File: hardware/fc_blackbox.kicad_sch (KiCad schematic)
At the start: 3 parts

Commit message: Library: every symbol, footprint and 3D model project-local (#28)
* Owner: board cleanup, Core placed on the board

Co-Authored-By: Claude Opus 5.5 <noreply@anthropic.com>

* Library: every symbol, footprint and 3D model project-local

- 3D models: 275 board model paths and 28 lib.pretty footprints pointed at
  KiCad's stock install or at ${OPENDRONE_LIB} (which this machine's KiCad sets
  to a path that does not exist, so 9 models were missing). All now resolve to
  ${KIPRJMOD}/lib.3dshapes; the three missing ones come from the repo's
  KiCad-Library submodule. .wrl replaced by the .step sibling where one exists.
- Symbols: the 14 stock symbols (Device, power, Connector, Connector_Generic,
  MCU_Espressif) copied into lib.kicad_sym from the schematic's own cache and
  relinked as lib:. Four lib symbols refreshed from the schematic (they still
  held the 8fa8d7b copies).
- Pruned: 11 unused footprints, 7 unused symbols, unreferenced model files.
- tools/localise_models.py and tools/localise_symbols.py keep it that way.
- Checks: board diff is model lines only; netlist identical; ERC 31 errors as
  before, lib_symbol_mismatch 9 -> 0.

Co-Authored-By: Claude Opus 5.5 <noreply@anthropic.com>

---------

Co-authored-by: Stan <stan@openaio.local>
Co-authored-by: Claude Opus 5.5 <noreply@anthropic.com>
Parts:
- C36: symbol Device:C -> lib:C
- R34: symbol Device:R -> lib:R
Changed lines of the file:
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@@
 	)
 	(symbol
-		(lib_id "Device:R")
+		(lib_id "lib:R")
 		(at 92.71 60.96 0)
 		(unit 1)
@@
 	)
 	(symbol
-		(lib_id "power:GND")
+		(lib_id "lib:GND")
 		(at 58.42 50.8 270)
 		(unit 1)
@@
 	)
 	(symbol
-		(lib_id "power:GND")
+		(lib_id "lib:GND")
 		(at 72.39 78.74 0)
 		(unit 1)
@@
 	)
 	(symbol
-		(lib_id "Device:C")
+		(lib_id "lib:C")
 		(at 63.5 50.8 270)
 		(unit 1)
@@
 	)
 	(symbol
-		(lib_id "power:+3V3")
+		(lib_id "lib:+3V3")
 		(at 92.71 57.15 0)
 		(unit 1)
@@
 	)
 	(symbol
-		(lib_id "power:+3V3")
+		(lib_id "lib:+3V3")
 		(at 72.39 50.8 0)
 		(unit 1)

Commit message: Owner: rerouting in progress; KiCad re-save of the sheets (netlist unchanged)
Co-Authored-By: Claude Opus 5.5 <noreply@anthropic.com>
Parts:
- renumbered Card2 to Card1
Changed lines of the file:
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@@
 		)
 		(instances
-			(project "OpenAIO-Base"
+			(project "OpenAIO"
 				(path "/fb88b6f9-ee39-4640-a9d4-04a17ceeac64/92d80a6e-4bd9-4df0-920d-da7b8cdc2925"
 					(reference "R34")
@@
 		(in_pos_files yes)
 		(dnp no)
-		(property "Reference" "Card2"
+		(property "Reference" "Card1"
 			(at 72.39 77.47 0)
 			(hide yes)
@@
 				)
 			)
-			(project "OpenAIO-Base"
+			(project "OpenAIO"
 				(path "/fb88b6f9-ee39-4640-a9d4-04a17ceeac64/92d80a6e-4bd9-4df0-920d-da7b8cdc2925"
 					(reference "Card1")
@@
 		)
 		(instances
-			(project "OpenAIO-Base"
+			(project "OpenAIO"
 				(path "/fb88b6f9-ee39-4640-a9d4-04a17ceeac64/92d80a6e-4bd9-4df0-920d-da7b8cdc2925"
 					(reference "#PWR0102")
@@
 		)
 		(instances
-			(project "OpenAIO-Base"
+			(project "OpenAIO"
 				(path "/fb88b6f9-ee39-4640-a9d4-04a17ceeac64/92d80a6e-4bd9-4df0-920d-da7b8cdc2925"
 					(reference "#PWR0104")
@@
 		)
 		(instances
-			(project "OpenAIO-Base"
+			(project "OpenAIO"
 				(path "/fb88b6f9-ee39-4640-a9d4-04a17ceeac64/92d80a6e-4bd9-4df0-920d-da7b8cdc2925"
 					(reference "C36")
@@
 		)
 		(instances
-			(project "OpenAIO-Base"
+			(project "OpenAIO"
 				(path "/fb88b6f9-ee39-4640-a9d4-04a17ceeac64/92d80a6e-4bd9-4df0-920d-da7b8cdc2925"
 					(reference "#PWR0286")
@@
 		)
 		(instances
-			(project "OpenAIO-Base"
+			(project "OpenAIO"
 				(path "/fb88b6f9-ee39-4640-a9d4-04a17ceeac64/92d80a6e-4bd9-4df0-920d-da7b8cdc2925"
 					(reference "#PWR0287")

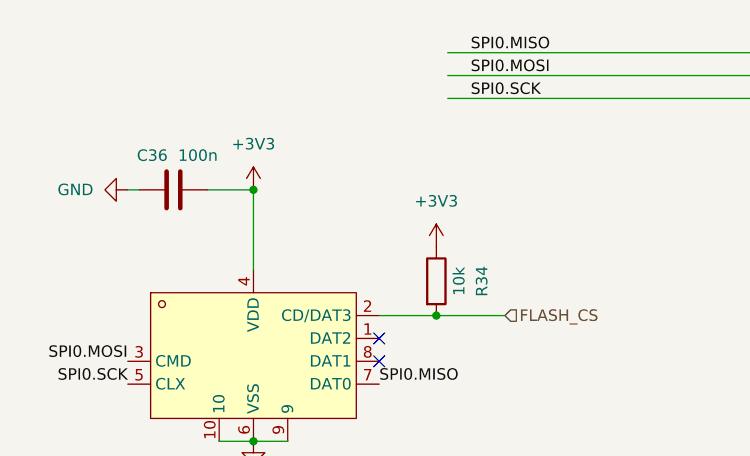
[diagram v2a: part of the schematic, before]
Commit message: One 3.3 V rail: U7 becomes TLV76733DRVR (1 A), U23 removed
- U7 LP5912-3.3DRVR (500 mA) -> TLV76733DRVR (1 A, LCSC C2848334, as on
  OpenESC-20x20), same WSON-6 2x2 land; SNS (pin 2) tied to OUT in the
  schematic and by a 0.25 mm jumper on B.Cu.
- U23 TLV75533 removed; the 17 +3V3 power symbols are +3.3V, and the board's
  +3V3 copper (24 tracks, 6 vias, 3 pours) moved onto +3.3V.
- Netlist: only U7 (value, MPN, LCSC, pin 2), U23 gone, +3V3 merged into +3.3V.
  ERC 31 errors as before. DRC: no new unconnected beyond the link the old
  +3V3 side now needs to U7.
- Docs: ROUTING.md rails and reroute step; firmware notes on the single rail
  (ISSUES I15 resolved).

Co-Authored-By: Claude Opus 5.5 <noreply@anthropic.com>
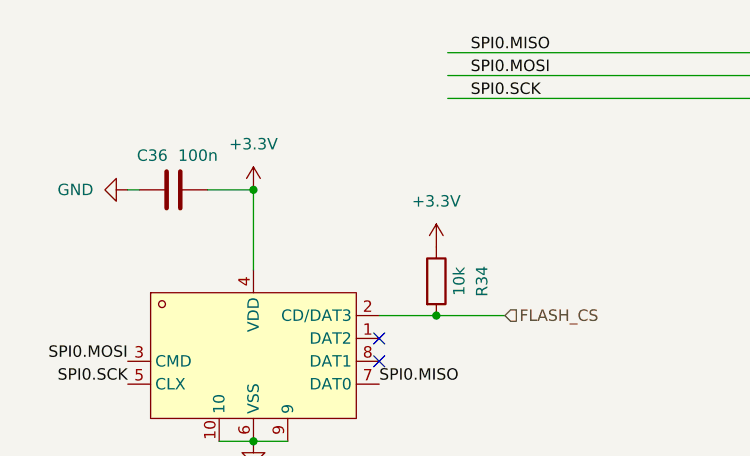
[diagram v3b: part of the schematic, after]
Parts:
- renumbered Card1 to Card2
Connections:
- net +3V3 renamed +3.3V
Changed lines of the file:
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@@
 		(in_pos_files yes)
 		(dnp no)
-		(property "Reference" "Card1"
+		(property "Reference" "Card2"
 			(at 72.39 77.47 0)
 			(hide yes)
@@
 	)
 	(symbol
-		(lib_id "lib:+3V3")
+		(lib_id "lib:+3.3V")
 		(at 92.71 57.15 0)
 		(unit 1)
@@
 			)
 		)
-		(property "Value" "+3V3"
+		(property "Value" "+3.3V"
 			(at 92.71 52.07 0)
 			(show_name no)
@@
 	)
 	(symbol
-		(lib_id "lib:+3V3")
+		(lib_id "lib:+3.3V")
 		(at 72.39 50.8 0)
 		(unit 1)
@@
 			)
 		)
-		(property "Value" "+3V3"
+		(property "Value" "+3.3V"
 			(at 72.39 45.72 0)
 			(show_name no)

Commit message: Owner: routing in progress
Co-Authored-By: Claude Opus 5.5 <noreply@anthropic.com>
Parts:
- renumbered Card2 to Card1
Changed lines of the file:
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@@
 		(in_pos_files yes)
 		(dnp no)
-		(property "Reference" "Card2"
+		(property "Reference" "Card1"
 			(at 72.39 77.47 0)
 			(hide yes)
